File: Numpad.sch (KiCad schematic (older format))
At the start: 56 parts, among them J1 AVR-ISP-6, SW1 SW_Push, U1 USBLC6-2SC6, U2 ATmega32U2-AU, Y1 16MHz

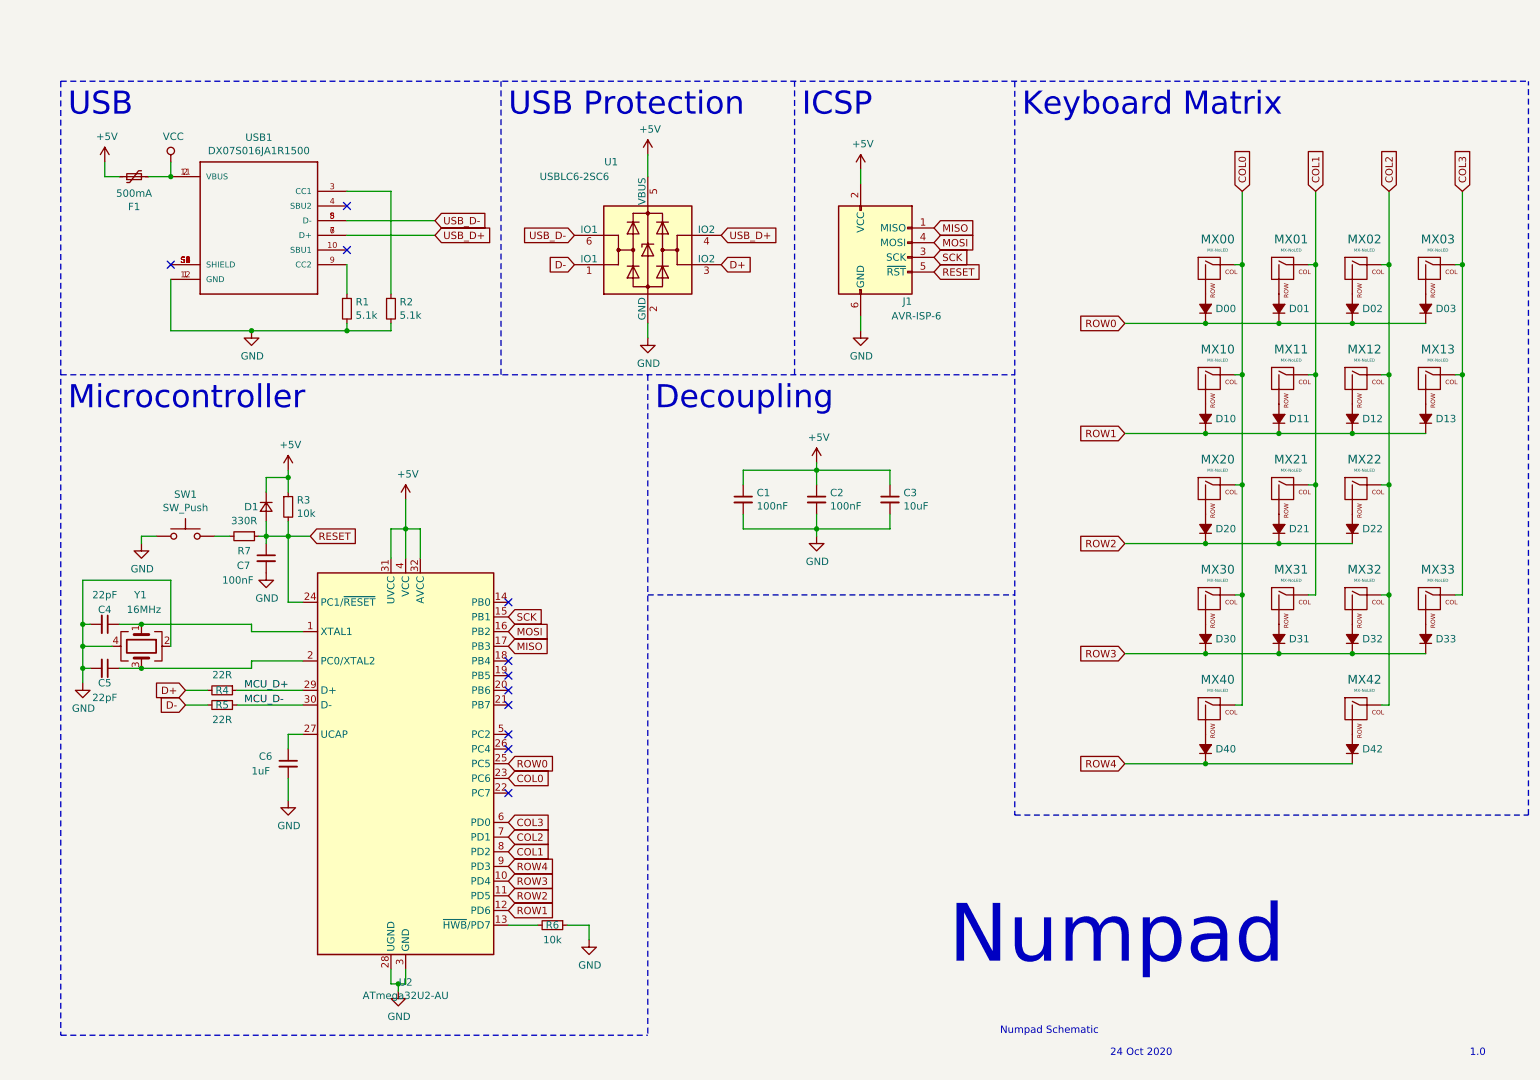
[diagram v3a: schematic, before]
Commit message: Fix issues with reset button and bootloader mode
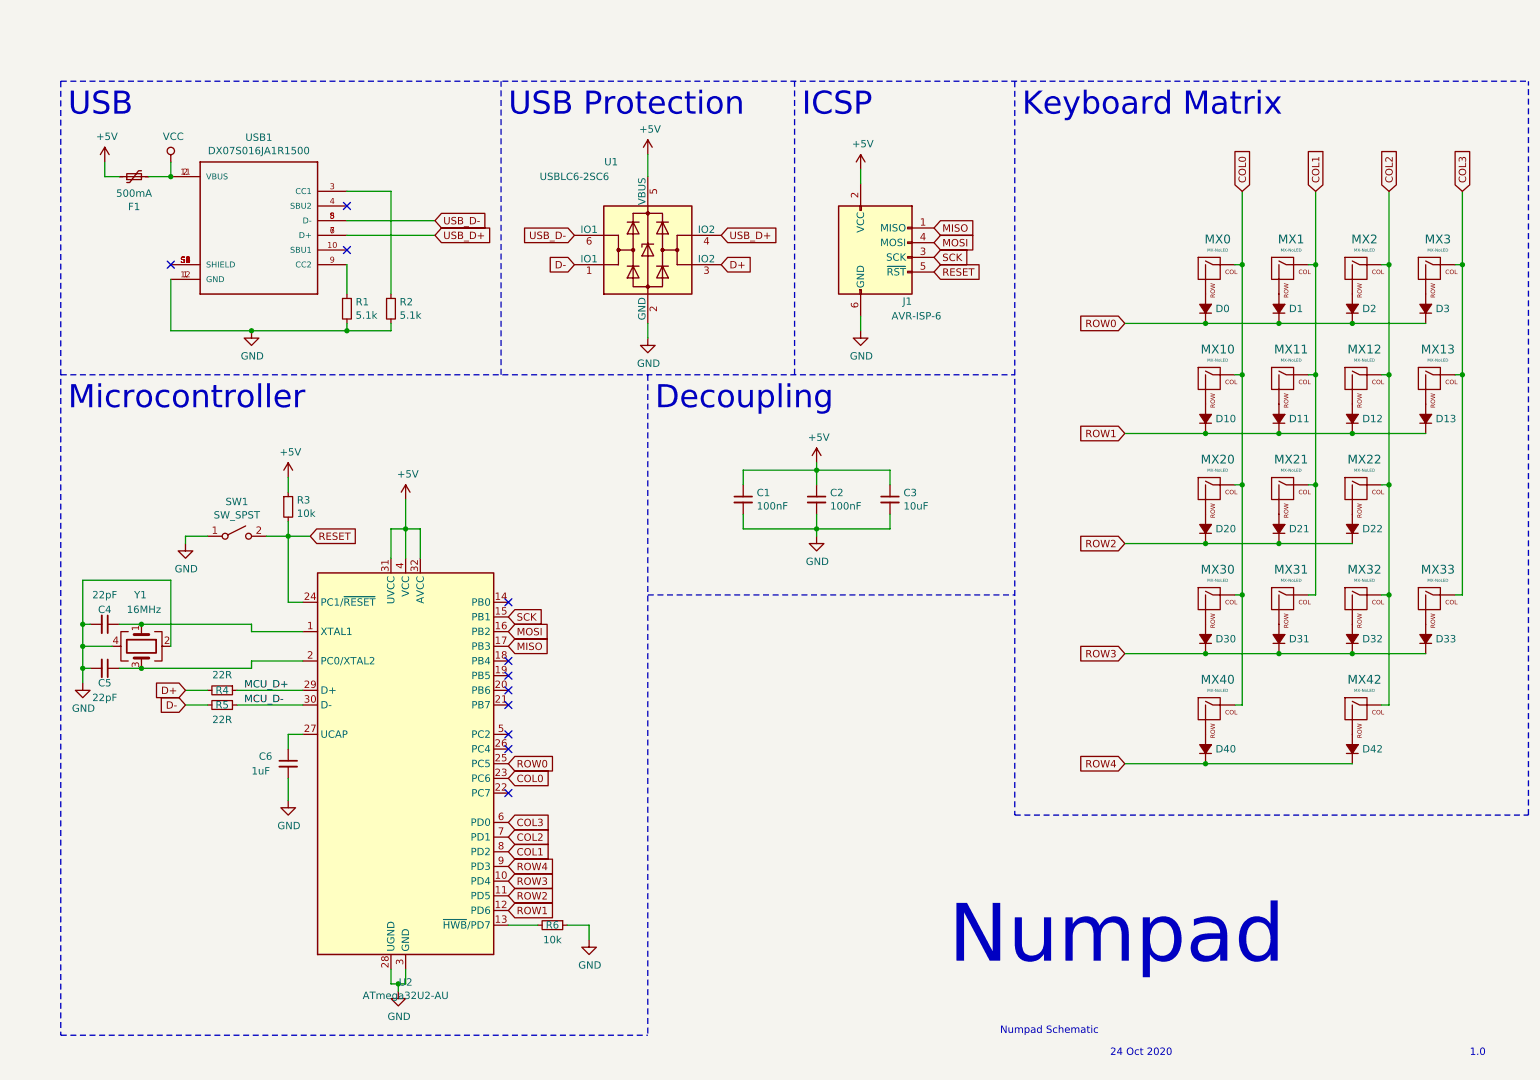
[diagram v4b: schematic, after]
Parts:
- removed C7: 100nF, Capacitor_SMD:C_0603_1608Metric, symbol Device:C_Small
- removed D1: D_Small, Diode_SMD:D_SOD-123, symbol Device:D_Small
- removed R7: 330R, Resistor_SMD:R_0603_1608Metric, symbol Device:R_Small
- removed SW1: SW_Push, Switches:TACTILE_SWITCH_SMD_5.2MM, symbol Switch:SW_Push
- added SW1: SW_SPST, Button_Switch_SMD:TACTILE_SWITCH_SPST_SMD_5.2MM, symbol Switch:SW_SPST
- renumbered D00 to D0, D01 to D1, D02 to D2, D03 to D3, MX00 to MX0, MX01 to MX1, MX02 to MX2, MX03 to MX3
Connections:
- net GND: now also SW1.1 (A)
- net RESET: now also SW1.2 (B)
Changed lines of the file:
@@
 EESchema Schematic File Version 4
-LIBS:Numpad-cache
 EELAYER 30 0
 EELAYER END
@@
 $EndDescr
 $Comp
-L MX_Alps_Hybrid:MX-NoLED MX03
+L MX_Alps_Hybrid:MX-NoLED MX3
 U 1 1 5F8C2530
 P 10350 2300
-F 0 "MX03" H 10383 2523 60  0000 C CNN
+F 0 "MX3" H 10383 2523 60  0000 C CNN
 F 1 "MX-NoLED" H 10383 2449 20  0000 C CNN
 F 2 "MX_Only:MXOnly-1U-NoLED" H 9725 2275 60  0001 C CNN
@@
 $EndComp
 $Comp
-L MX_Alps_Hybrid:MX-NoLED MX02
+L MX_Alps_Hybrid:MX-NoLED MX2
 U 1 1 5F8C2536
 P 9850 2300
-F 0 "MX02" H 9883 2523 60  0000 C CNN
+F 0 "MX2" H 9883 2523 60  0000 C CNN
 F 1 "MX-NoLED" H 9883 2449 20  0000 C CNN
 F 2 "MX_Only:MXOnly-1U-NoLED" H 9225 2275 60  0001 C CNN
@@
 $EndComp
 $Comp
-L MX_Alps_Hybrid:MX-NoLED MX01
+L MX_Alps_Hybrid:MX-NoLED MX1
 U 1 1 5F8C253C
 P 9350 2300
-F 0 "MX01" H 9383 2523 60  0000 C CNN
+F 0 "MX1" H 9383 2523 60  0000 C CNN
 F 1 "MX-NoLED" H 9383 2449 20  0000 C CNN
 F 2 "MX_Only:MXOnly-1U-NoLED" H 8725 2275 60  0001 C CNN
@@
 $EndComp
 $Comp
-L MX_Alps_Hybrid:MX-NoLED MX00
+L MX_Alps_Hybrid:MX-NoLED MX0
 U 1 1 5F8C2542
 P 8850 2300
-F 0 "MX00" H 8883 2523 60  0000 C CNN
+F 0 "MX0" H 8883 2523 60  0000 C CNN
 F 1 "MX-NoLED" H 8883 2449 20  0000 C CNN
 F 2 "MX_Only:MXOnly-1U-NoLED" H 8225 2275 60  0001 C CNN
@@
 Connection ~ 10050 4500
 $Comp
-L Device:D_Small_ALT D00
+L Device:D_Small_ALT D0
 U 1 1 5F91D984
 P 8800 2550
-F 0 "D00" V 8800 2482 50  0000 R CNN
+F 0 "D0" V 8800 2482 50  0000 R CNN
 F 1 "D_Small_ALT" V 8755 2482 50  0001 R CNN
 F 2 "Diode_SMD:D_SOD-123" V 8800 2550 50  0001 C CNN
@@
 $EndComp
 $Comp
-L Device:D_Small_ALT D01
+L Device:D_Small_ALT D1
 U 1 1 5F91E578
 P 9300 2550
-F 0 "D01" V 9300 2482 50  0000 R CNN
+F 0 "D1" V 9300 2482 50  0000 R CNN
 F 1 "D_Small_ALT" V 9255 2482 50  0001 R CNN
 F 2 "Diode_SMD:D_SOD-123" V 9300 2550 50  0001 C CNN
@@
 $EndComp
 $Comp
-L Device:D_Small_ALT D02
+L Device:D_Small_ALT D2
 U 1 1 5F91EB06
 P 9800 2550
-F 0 "D02" V 9800 2482 50  0000 R CNN
+F 0 "D2" V 9800 2482 50  0000 R CNN
 F 1 "D_Small_ALT" V 9755 2482 50  0001 R CNN
 F 2 "Diode_SMD:D_SOD-123" V 9800 2550 50  0001 C CNN
@@
 $EndComp
 $Comp
-L Device:D_Small_ALT D03
+L Device:D_Small_ALT D3
 U 1 1 5F91F207
 P 10300 2550
-F 0 "D03" V 10300 2482 50  0000 R CNN
+F 0 "D3" V 10300 2482 50  0000 R CNN
 F 1 "D_Small_ALT" V 10255 2482 50  0001 R CNN
 F 2 "Diode_SMD:D_SOD-123" V 10300 2550 50  0001 C CNN
@@
 Wire Wire Line
 	2550 4100 2700 4100
-$Comp
-L power:GND #PWR0115
-U 1 1 5F9D36E9
-P 2400 4350
-F 0 "#PWR0115" H 2400 4100 50  0001 C CNN
-F 1 "GND" H 2405 4177 50  0000 C CNN
-F 2 "" H 2400 4350 50  0001 C CNN
-F 3 "" H 2400 4350 50  0001 C CNN
-	1    2400 4350
-	1    0    0    -1
-$EndComp
-Wire Wire Line
-	2400 4150 2400 4100
-$Comp
-L Device:C_Small C7
-U 1 1 5F9CBBBB
-P 2400 4250
-F 0 "C7" H 2200 4200 50  0000 L CNN
-F 1 "100nF" H 2100 4100 50  0000 L CNN
-F 2 "Capacitor_SMD:C_0603_1608Metric" H 2400 4250 50  0001 C CNN
-F 3 "~" H 2400 4250 50  0001 C CNN
-	1    2400 4250
-	1    0    0    -1
-$EndComp
-Wire Wire Line
-	2150 4100 2050 4100
-Connection ~ 2400 4100
-Wire Wire Line
-	2400 4100 2350 4100
-Wire Wire Line
-	2400 4100 2550 4100
-$Comp
-L Device:R_Small R7
-U 1 1 5F9ADB55
-P 2250 4100
-F 0 "R7" V 2350 4100 50  0000 C CNN
-F 1 "330R" V 2145 4100 50  0000 C CNN
-F 2 "Resistor_SMD:R_0603_1608Metric" H 2250 4100 50  0001 C CNN
-F 3 "~" H 2250 4100 50  0001 C CNN
-	1    2250 4100
-	0    1    1    0
-$EndComp
-Wire Wire Line
-	2400 4000 2400 4100
-Wire Wire Line
-	2550 3700 2550 3800
-Connection ~ 2550 3700
-Wire Wire Line
-	2400 3700 2550 3700
-Wire Wire Line
-	2400 3800 2400 3700
-$Comp
-L Device:D_Small D1
-U 1 1 5F987CCC
-P 2400 3900
-F 0 "D1" V 2400 3750 50  0000 L CNN
-F 1 "D_Small" V 2450 3550 50  0001 L CNN
-F 2 "Diode_SMD:D_SOD-123" V 2400 3900 50  0001 C CNN
-F 3 "~" V 2400 3900 50  0001 C CNN
-	1    2400 3900
-	0    1    1    0
-$EndComp
-Connection ~ 2550 4100
 Wire Wire Line
 	2550 4100 2550 4550
@@
 F 3 "http://ww1.microchip.com/downloads/en/DeviceDoc/doc7799.pdf" H 3350 5650 50  0001 C CNN
 	1    3350 5650
-	1    0    0    -1
-$EndComp
-$Comp
-L power:GND #PWR0113
-U 1 1 5F9628D3
-P 1550 4150
-F 0 "#PWR0113" H 1550 3900 50  0001 C CNN
-F 1 "GND" H 1555 3977 50  0000 C CNN
-F 2 "" H 1550 4150 50  0001 C CNN
-F 3 "" H 1550 4150 50  0001 C CNN
-	1    1550 4150
 	1    0    0    -1
 $EndComp
@@
 	1    0    0    -1
 $EndComp
-$Comp
-L power:+5V #PWR0108
-U 1 1 5FA3D663
-P 2550 3650
-F 0 "#PWR0108" H 2550 3500 50  0001 C CNN
-F 1 "+5V" H 2565 3823 50  0000 C CNN
-F 2 "" H 2550 3650 50  0001 C CNN
-F 3 "" H 2550 3650 50  0001 C CNN
-	1    2550 3650
-	1    0    0    -1
-$EndComp
-Wire Wire Line
-	2550 3650 2550 3700
-Wire Wire Line
-	2550 4000 2550 4100
-$Comp
-L Device:R_Small R3
-U 1 1 5FA343DC
-P 2550 3900
-F 0 "R3" H 2609 3946 50  0000 L CNN
-F 1 "10k" H 2609 3855 50  0000 L CNN
-F 2 "Resistor_SMD:R_0603_1608Metric" H 2550 3900 50  0001 C CNN
-F 3 "~" H 2550 3900 50  0001 C CNN
-F 4 "C25744" H 2550 3900 50  0001 C CNN "LCSC"
-	1    2550 3900
-	1    0    0    -1
-$EndComp
-Wire Wire Line
-	1550 4100 1650 4100
-Wire Wire Line
-	1550 4150 1550 4100
 Wire Wire Line
 	2550 4550 2650 4550
@@
 Wire Wire Line
 	1550 4700 2300 4700
-$Comp
-L Switch:SW_Push SW1
-U 1 1 5FA19194
-P 1850 4100
-F 0 "SW1" H 1850 4385 50  0000 C CNN
-F 1 "SW_Push" H 1850 4294 50  0000 C CNN
-F 2 "Switches:TACTILE_SWITCH_SMD_5.2MM" H 1850 4300 50  0001 C CNN
-F 3 "~" H 1850 4300 50  0001 C CNN
-F 4 "C318884" H 1850 4100 50  0001 C CNN "LCSC"
-	1    1850 4100
-	1    0    0    -1
-$EndComp
 Connection ~ 1150 4700
 Wire Wire Line
@@
 Text Notes 7550 1250 0    157  ~ 0
 Keyboard Matrix
+Wire Wire Line
+	1850 4150 1850 4100
+$Comp
+L power:GND #PWR0113
+U 1 1 5F9628D3
+P 1850 4150
+F 0 "#PWR0113" H 1850 3900 50  0001 C CNN
+F 1 "GND" H 1855 3977 50  0000 C CNN
+F 2 "" H 1850 4150 50  0001 C CNN
+F 3 "" H 1850 4150 50  0001 C CNN
+	1    1850 4150
+	1    0    0    -1
+$EndComp
+Connection ~ 2550 4100
+$Comp
+L Device:R_Small R3
+U 1 1 5FA343DC
+P 2550 3900
+F 0 "R3" H 2609 3946 50  0000 L CNN
+F 1 "10k" H 2609 3855 50  0000 L CNN
+F 2 "Resistor_SMD:R_0603_1608Metric" H 2550 3900 50  0001 C CNN
+F 3 "~" H 2550 3900 50  0001 C CNN
+F 4 "C25744" H 2550 3900 50  0001 C CNN "LCSC"
+	1    2550 3900
+	1    0    0    -1
+$EndComp
+Wire Wire Line
+	2550 4000 2550 4100
+$Comp
+L power:+5V #PWR0108
+U 1 1 5FA3D663
+P 2550 3700
+F 0 "#PWR0108" H 2550 3550 50  0001 C CNN
+F 1 "+5V" H 2565 3873 50  0000 C CNN
+F 2 "" H 2550 3700 50  0001 C CNN
+F 3 "" H 2550 3700 50  0001 C CNN
+	1    2550 3700
+	1    0    0    -1
+$EndComp
+Wire Wire Line
+	2550 3700 2550 3800
+$Comp
+L Switch:SW_SPST SW1
+U 1 1 60068061
+P 2200 4100
+F 0 "SW1" H 2200 4335 50  0000 C CNN
+F 1 "SW_SPST" H 2200 4244 50  0000 C CNN
+F 2 "Button_Switch_SMD:TACTILE_SWITCH_SPST_SMD_5.2MM" H 2200 4100 50  0001 C CNN
+F 3 "~" H 2200 4100 50  0001 C CNN
+	1    2200 4100
+	1    0    0    -1
+$EndComp
+Wire Wire Line
+	1850 4100 2000 4100
+Wire Wire Line
+	2400 4100 2550 4100
 $EndSCHEMATC
